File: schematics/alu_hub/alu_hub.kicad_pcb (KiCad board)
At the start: 2 copper layers, 100 x 91.1 mm, 24 parts, among them U1 74LS574, U10 74LS02, U2 74LS245, U3 74LS02, U4 74LS181, U5 74LS181, U6 74LS574, U7 74LS245, U8 74LS245, U9 74LS02

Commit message: silklayer check
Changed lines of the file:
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@@
 		(tags "THT DIP DIL PDIP 2.54mm 7.62mm 300mil Socket LongPads")
 		(property "Reference" "U8"
-			(at 3.81 -2.33 90)
+			(at 5.045 -2.445 90)
 			(layer "F.SilkS")
 			(effects
@@
 		(tags "C Disc series Radial pin pitch 2.50mm diameter 5mm width 2.5mm Capacitor")
 		(property "Reference" "C5"
-			(at 1.25 -2.5 90)
+			(at 0.37 -2.56 90)
 			(layer "F.SilkS")
 			(effects
@@
 		(tags "THT DIP DIL PDIP 2.54mm 7.62mm 300mil Socket LongPads")
 		(property "Reference" "U7"
-			(at 3.81 -2.33 90)
+			(at 2.8712 -2.445 90)
 			(layer "F.SilkS")
 			(effects
@@
 		(tags "C Radial series Radial pin pitch 2.50mm diameter 6.3mm height 5mm Non-Polar Electrolytic Capacitor")
 		(property "Reference" "C11"
-			(at 1.25 -4.4 0)
+			(at 5.7 2.8 0)
 			(layer "F.SilkS")
 			(effects
@@
 		(tags "THT DIP DIL PDIP 2.54mm 7.62mm 300mil Socket LongPads")
 		(property "Reference" "U1"
-			(at 3.81 -2.33 90)
+			(at 0.35 -2.695 90)
 			(layer "F.SilkS")
 			(effects
@@
 		(tags "THT DIP DIL PDIP 2.54mm 15.24mm 600mil Socket LongPads")
 		(property "Reference" "U4"
-			(at 7.62 -2.33 90)
+			(at 4.515 -2.72 90)
 			(layer "F.SilkS")
 			(effects
@@
 		(tags "PCIe")
 		(property "Reference" "BC1"
-			(at 5 -3.5 0)
+			(at 7.5 -3.75 0)
 			(layer "F.SilkS")
 			(effects
@@
 		(tags "THT DIP DIL PDIP 2.54mm 7.62mm 300mil Socket LongPads")
 		(property "Reference" "U10"
-			(at 3.81 -2.33 90)
+			(at 2.07 -2.58 90)
 			(layer "F.SilkS")
 			(effects
@@
 		(tags "THT DIP DIL PDIP 2.54mm 7.62mm 300mil Socket LongPads")
 		(property "Reference" "U6"
-			(at 3.81 -2.33 90)
+			(at 1.9475 -2.445 90)
 			(layer "F.SilkS")
 			(effects
@@
 	)
 	(segment
-		(start 143.475 85.425)
-		(end 141.64 85.425)
-		(width 0.2)
-		(layer "F.Cu")
-		(net 32)
-	)
-	(segment
 		(start 161 137.325)
 		(end 162.226 136.099)
@@
 	)
 	(segment
-		(start 141.64 85.425)
-		(end 133.2 76.985)
-		(width 0.2)
-		(layer "F.Cu")
-		(net 32)
-	)
-	(segment
 		(start 174.761049 87.8265)
 		(end 173.848951 87.8265)
@@
 	)
 	(segment
+		(start 143.475 85.425)
+		(end 140.925 85.425)
+		(width 0.2)
+		(layer "F.Cu")
+		(net 32)
+	)
+	(segment
+		(start 140.925 85.425)
+		(end 133.2 77.7)
+		(width 0.2)
+		(layer "F.Cu")
+		(net 32)
+	)
+	(segment
 		(start 162.226 136.099)
 		(end 169.851 136.099)
@@
 		(width 0.2)
 		(layer "F.Cu")
+		(net 32)
+	)
+	(segment
+		(start 133.2 77.7)
+		(end 133.2 76.985)
+		(width 0.2)
+		(layer "F.Cu")

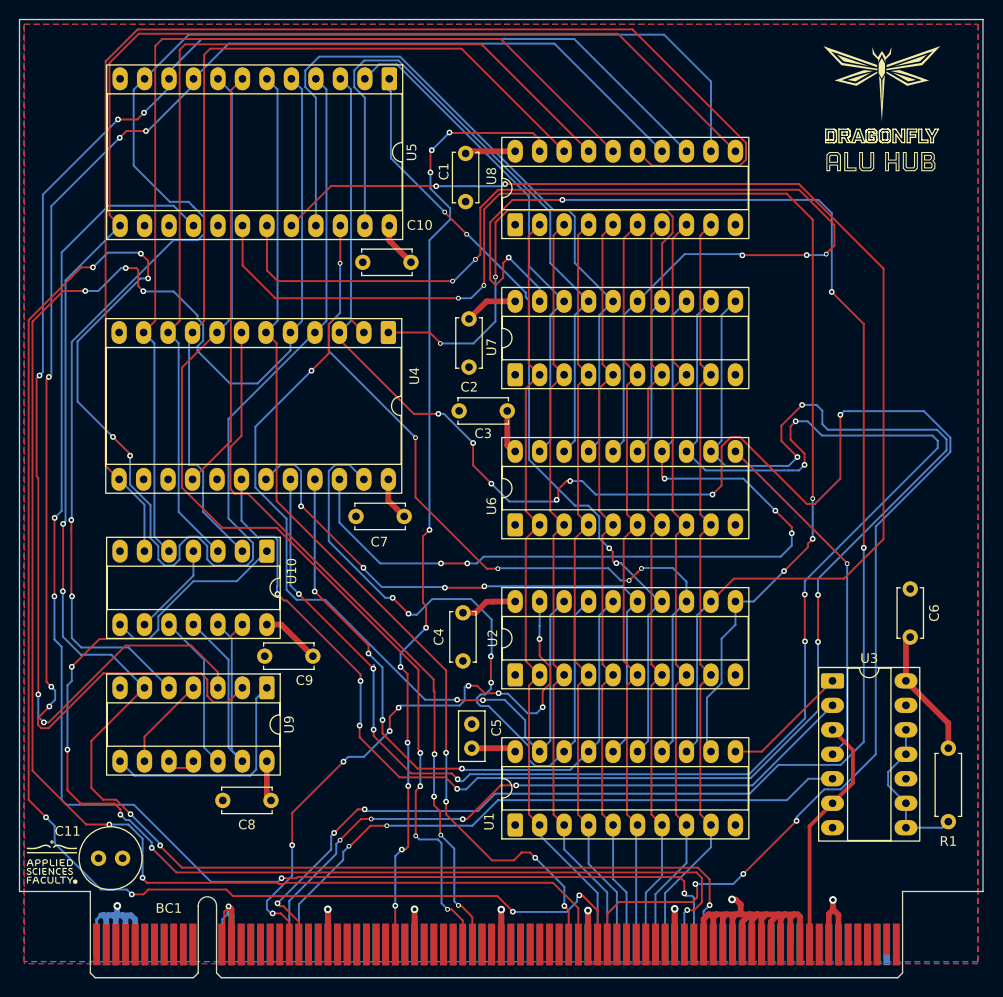
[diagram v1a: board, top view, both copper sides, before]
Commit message: fix(alu): changed vcc gnd connection  + clearence of cooper zones
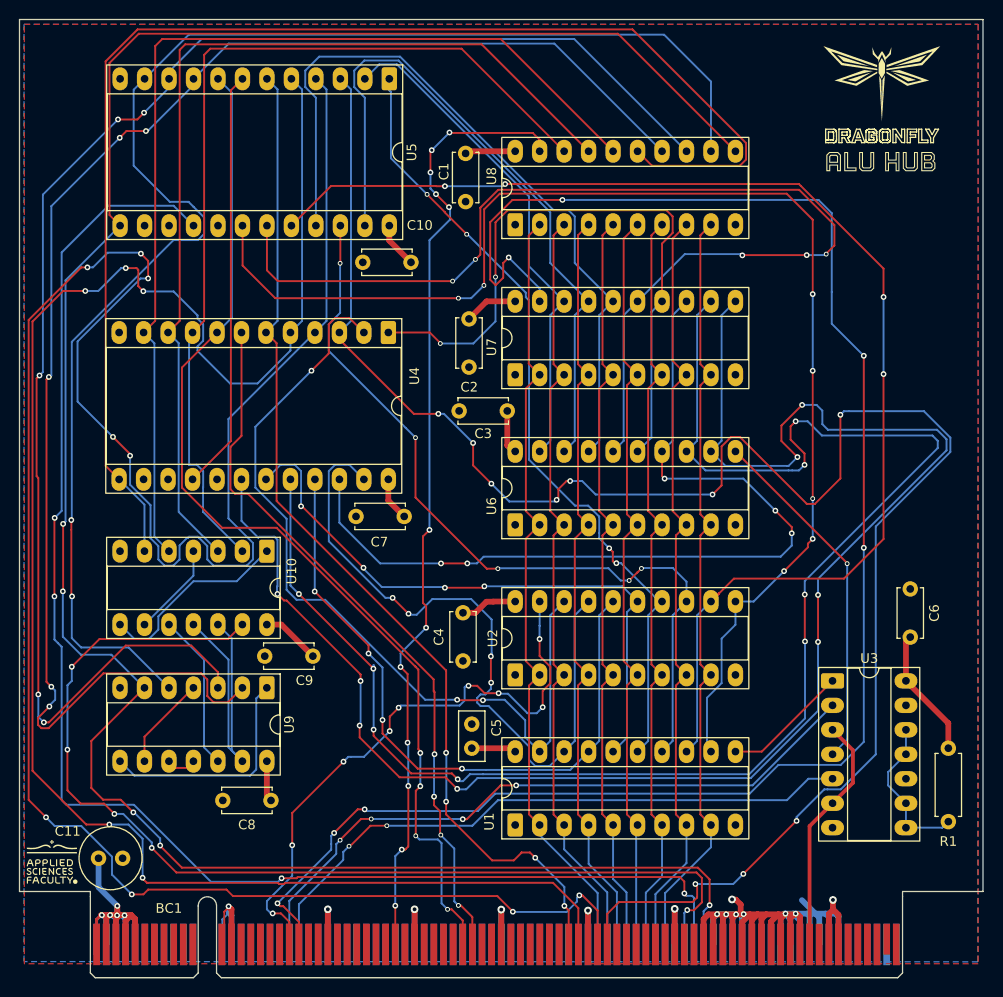
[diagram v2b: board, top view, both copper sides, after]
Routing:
- net GND: track 105.5 -> 155.9 mm, vias 8 -> 14
- net VCC: track 78.8 -> 104.9 mm, vias 1 -> 5
- net Net-(BC1-~{RALU}): vias 10 -> 12
- net /HIGH7: vias 5 -> 7
- net /HIGH6: vias 2 -> 4

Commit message: fix(alu, core2, interface): vcc conection some routing issues
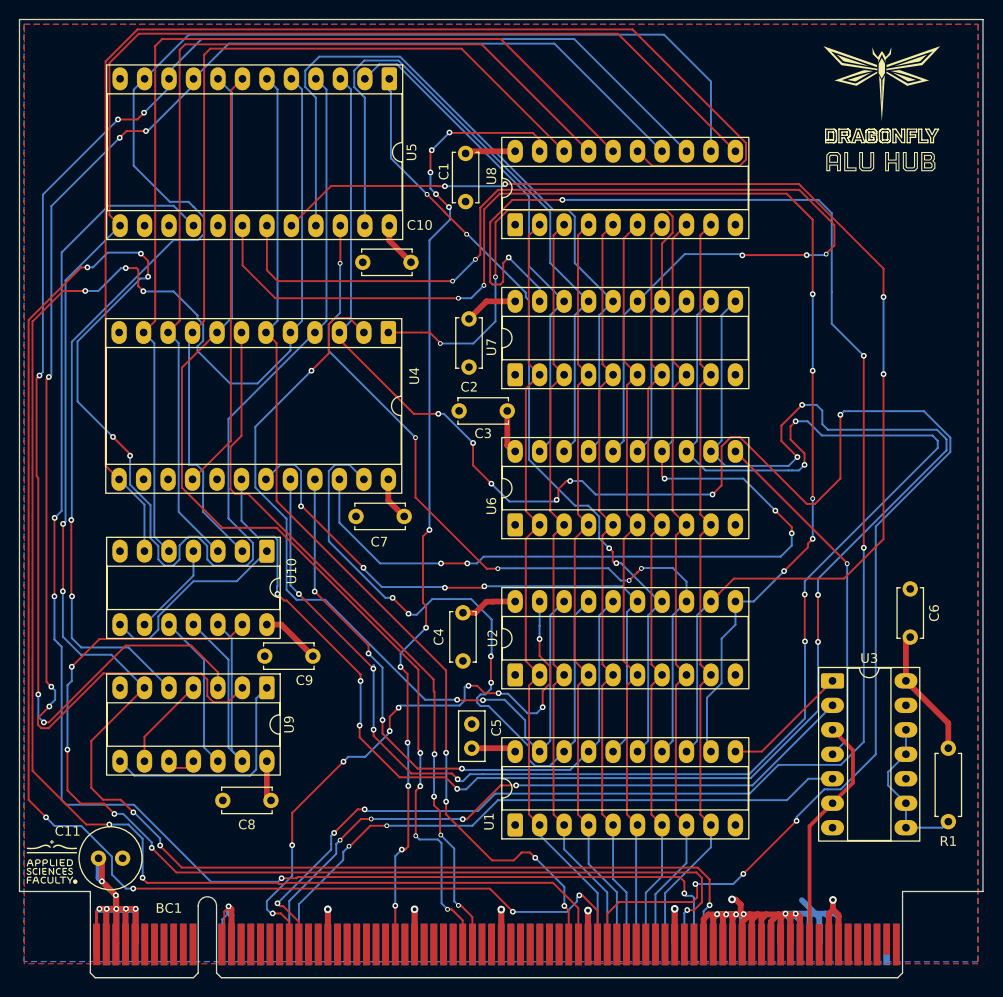
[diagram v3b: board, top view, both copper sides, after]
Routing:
- net VCC: track 104.9 -> 115.7 mm, vias 5 -> 7
- net Net-(BC1-ALUS2): track 244.0 -> 243.5 mm

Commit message: fix: removed in control pins daisy chains
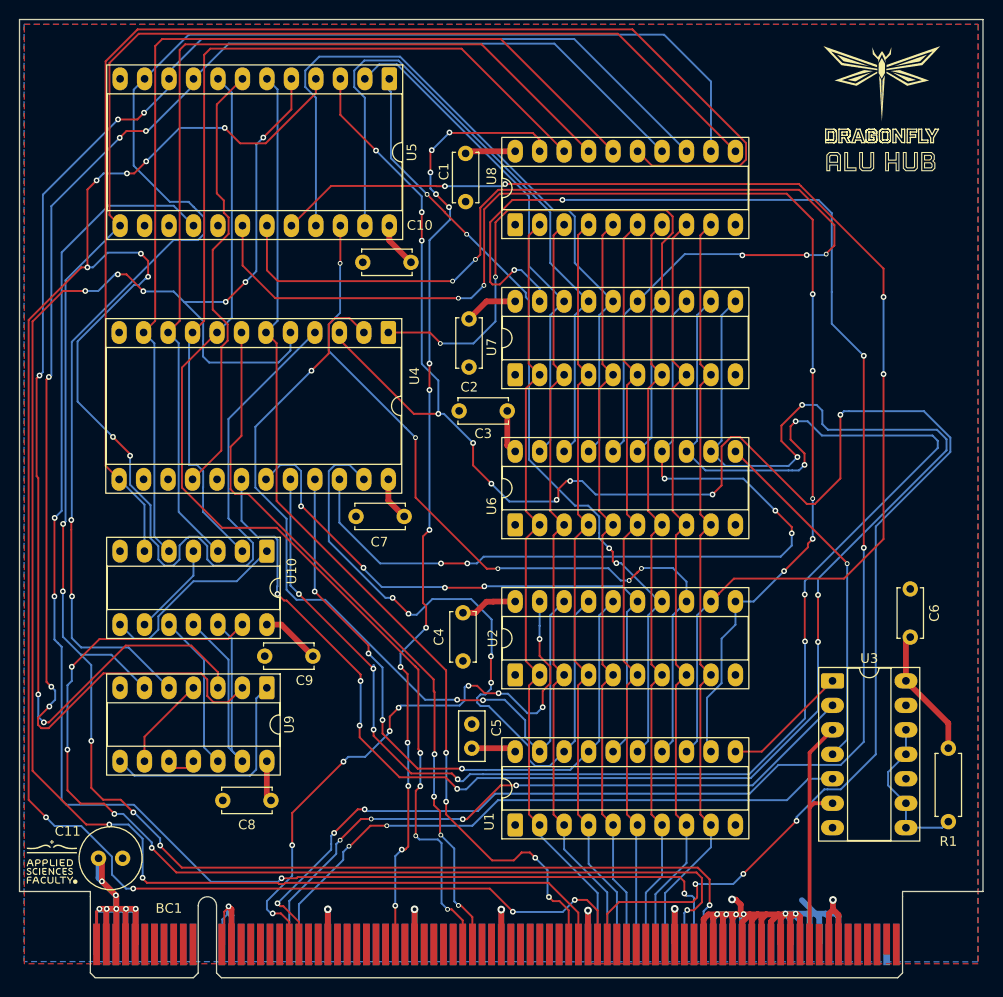
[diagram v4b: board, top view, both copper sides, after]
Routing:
- net Net-(BC1-ALUS3): track 193.8 -> 205.5 mm, vias 10 -> 13
- net Net-(BC1-ALUS2): track 243.5 -> 254.3 mm, vias 9 -> 13
- net Net-(U4-Cn+4): track 43.7 -> 46.0 mm
- net Net-(BC1-~{RARGL}): track 183.8 -> 181.6 mm
- net Net-(BC1-ALUSO): track 232.7 -> 234.3 mm, vias 5 -> 6
- net Net-(BC1-ALUS1): track 183.7 -> 182.6 mm, vias 5 -> 8
- net Net-(BC1-~{CLK}): track 25.0 -> 25.8 mm
- net Net-(BC1-~{RALU}): vias 12 -> 14

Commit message: fix(alu): vcc conn
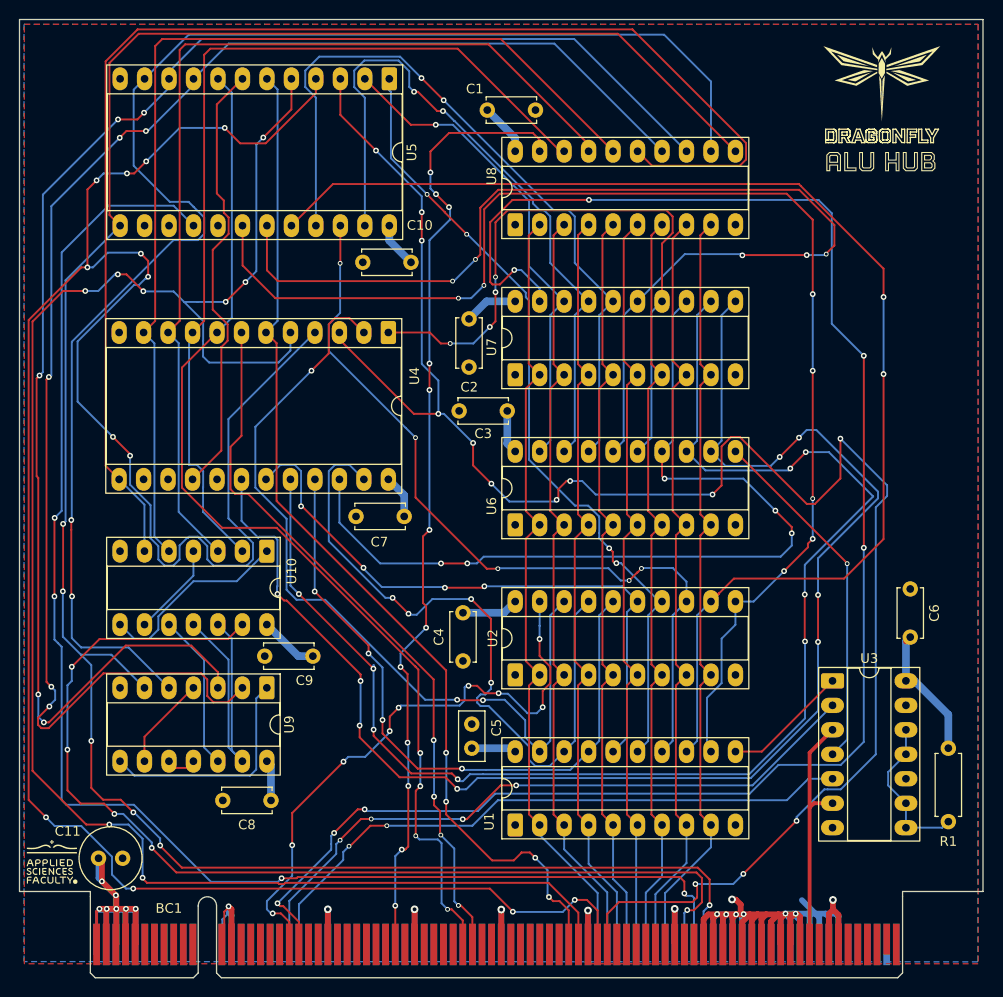
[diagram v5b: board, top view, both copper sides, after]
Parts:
- moved C1 12.0 mm to (153.6, 53.9), turned to 180 degrees
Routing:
- net /LOW7: track 171.0 -> 150.6 mm
- net /LOW6: track 165.8 -> 146.0 mm
- net Net-(BC1-ALUS3): track 205.5 -> 189.5 mm
- net VCC: track 115.7 -> 117.7 mm
- net /LOW0: track 52.4 -> 50.9 mm, vias 0 -> 1
- net /LOW1: track 71.4 -> 72.3 mm, vias 0 -> 2
- net /LOW4: track 68.0 -> 67.9 mm, vias 2 -> 4
- net Net-(BC1-~{RALU}): vias 14 -> 12
- net /HIGH6: track 133.4 -> 133.3 mm, vias 4 -> 2
- net /LOW2: vias 0 -> 2

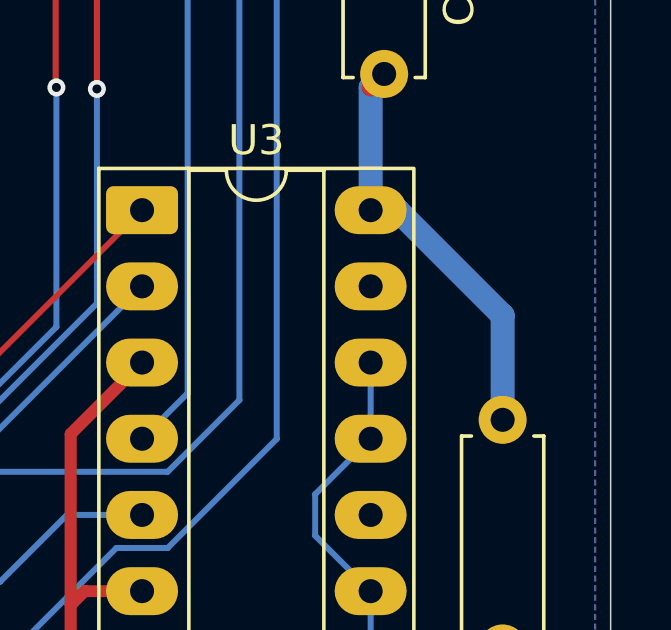
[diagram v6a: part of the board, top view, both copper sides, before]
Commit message: fix(register_accum): fixed the data to y shape connection removed the vcc from the resistor
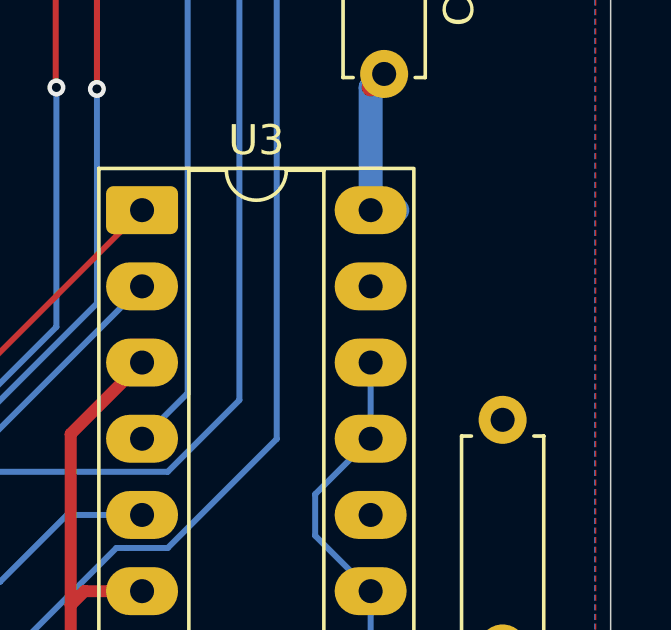
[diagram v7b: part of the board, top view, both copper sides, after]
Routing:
- net VCC: track 117.7 -> 109.2 mm
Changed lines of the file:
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@@
-	)
-	(segment
-		(start 196.4 116.65)
-		(end 196.4 120.13)
-		(width 0.8)
-		(layer "B.Cu")
-		(net 2)
 	)
 	(segment
@@
 		(layer "B.Cu")
 		(net 2)
-	)
-	(segment
-		(start 192.89 113.14)
-		(end 196.4 116.65)
-		(width 0.8)
-		(layer "B.Cu")
-		(net 2)

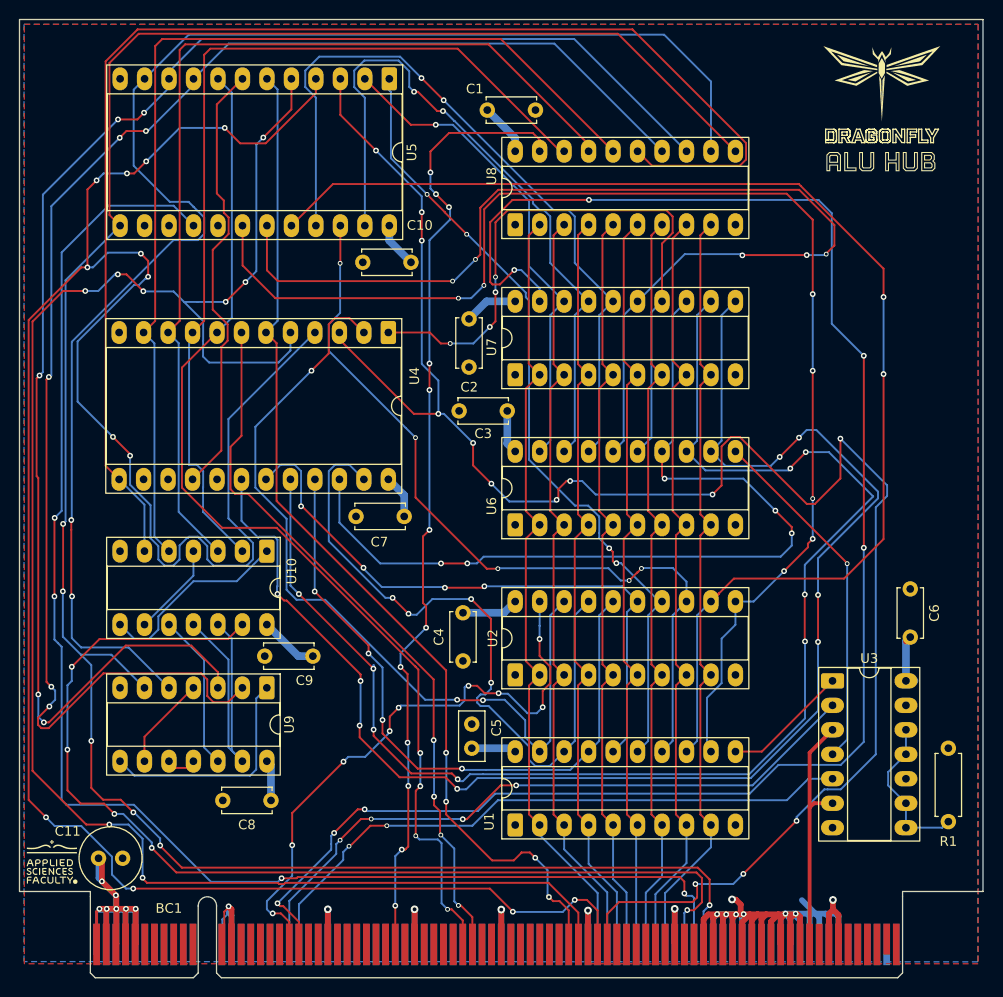
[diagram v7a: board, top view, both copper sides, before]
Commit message: feat(alu): added tp to alu
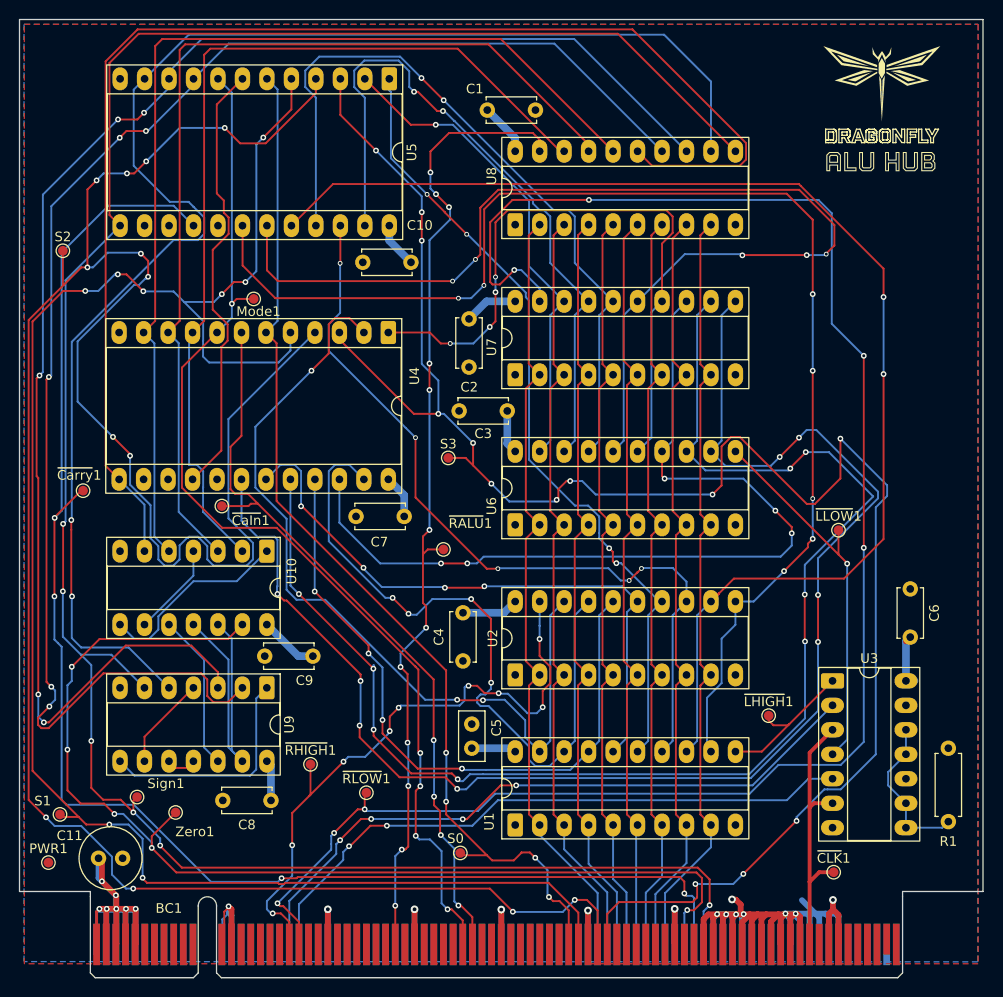
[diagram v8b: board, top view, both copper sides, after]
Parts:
- added Mode1: Mode, TestPoint:TestPoint_Pad_D1.0mm, F.Cu at (124.3, 73.5)
- added PWR1: Power, TestPoint:TestPoint_Pad_D1.0mm, F.Cu at (103.0, 132.0)
- added S0: S0, TestPoint:TestPoint_Pad_D1.0mm, F.Cu at (145.8, 131.0)
- added S1: S1, TestPoint:TestPoint_Pad_D1.0mm, F.Cu at (104.2, 127.0)
- added S2: S2, TestPoint:TestPoint_Pad_D1.0mm, F.Cu at (104.5, 68.5)
- added S3: S3, TestPoint:TestPoint_Pad_D1.0mm, F.Cu at (144.5, 90.0)
- added Sign1: Sign, TestPoint:TestPoint_Pad_D1.0mm, F.Cu at (112.2, 125.2)
- added Zero1: Zero, TestPoint:TestPoint_Pad_D1.0mm, F.Cu at (116.2, 126.8)
- added ~{CLK}1: ~{Clock}, TestPoint:TestPoint_Pad_D1.0mm, F.Cu at (184.5, 133.0)
- added ~{CaIn}1: ~{CaIn}, TestPoint:TestPoint_Pad_D1.0mm, F.Cu at (121.0, 95.0)
- added ~{Carry}1: ~{Carry}, TestPoint:TestPoint_Pad_D1.0mm, F.Cu at (106.6, 93.4)
- added ~{LHIGH}1: ~{LoadHigh}, TestPoint:TestPoint_Pad_D1.0mm, F.Cu at (177.8, 116.8)
- added ~{LLOW}1: ~{LoadLow}, TestPoint:TestPoint_Pad_D1.0mm, F.Cu at (185.0, 97.5)
- added ~{RALU}1: ~{ReadALU}, TestPoint:TestPoint_Pad_D1.0mm, F.Cu at (144.0, 99.5)
- added ~{RHIGH}1: ~{ReadHigh}, TestPoint:TestPoint_Pad_D1.0mm, F.Cu at (130.2, 121.8)
- added ~{RLOW}1: ~{ReadLow}, TestPoint:TestPoint_Pad_D1.0mm, F.Cu at (136.0, 124.8)
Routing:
- net Net-(BC1-ALUZO): track 110.6 -> 115.3 mm
- net Net-(BC1-~{ALUCO}): track 150.2 -> 154.3 mm
- net Net-(BC1-~{ALUCI}): track 75.3 -> 79.2 mm
- net Net-(BC1-ALUS2): track 254.3 -> 257.9 mm
- net Net-(BC1-~{RARGH}): track 62.7 -> 66.1 mm
- net Net-(BC1-~{CLK}): track 25.8 -> 28.8 mm
- net Net-(BC1-ALUS3): track 189.5 -> 192.4 mm
- net Net-(U1-Cp): track 13.1 -> 16.0 mm
- net Net-(BC1-ALUS0): track 107.7 -> 110.6 mm
- net Net-(U6-Cp): track 36.9 -> 39.4 mm
- net Net-(BC1-~{RALU}): track 100.3 -> 102.6 mm
- net Net-(BC1-ALUS1): track 182.6 -> 184.7 mm
- net Net-(BC1-ALUM): track 109.8 -> 111.8 mm, vias 4 -> 5
- net Net-(BC1-~{RARGL}): track 181.6 -> 183.4 mm
- net Net-(BC1-ALUSO): track 234.3 -> 236.0 mm
